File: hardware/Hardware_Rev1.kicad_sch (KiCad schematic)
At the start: 149 parts, among them J1 RJ45_LED_Shielded, J2 6P6C, Q1 BSS138, Q10 IRF7606PBF, Q11 IRF7606PBF, Q12 IRF7606PBF, Q13 BSS138, Q14 BSS138, Q15 BSS138, Q16 IRF7606PBF, Q17 IRF7606PBF, Q18 IRF7606PBF, Q19 BSS138, Q2 BSS138, Q20 BSS138, Q21 BSS138, Q22 IRF7606PBF, Q23 IRF7606PBF, Q24 IRF7606PBF, Q3 BSS138, Q4 IRF7606PBF, Q5 IRF7606PBF, Q6 IRF7606PBF, Q7 BSS138, Q8 BSS138, Q9 BSS138, U3 OKI, U5 TSR_1-2450, U6 Teensy4.1_DEV-16771

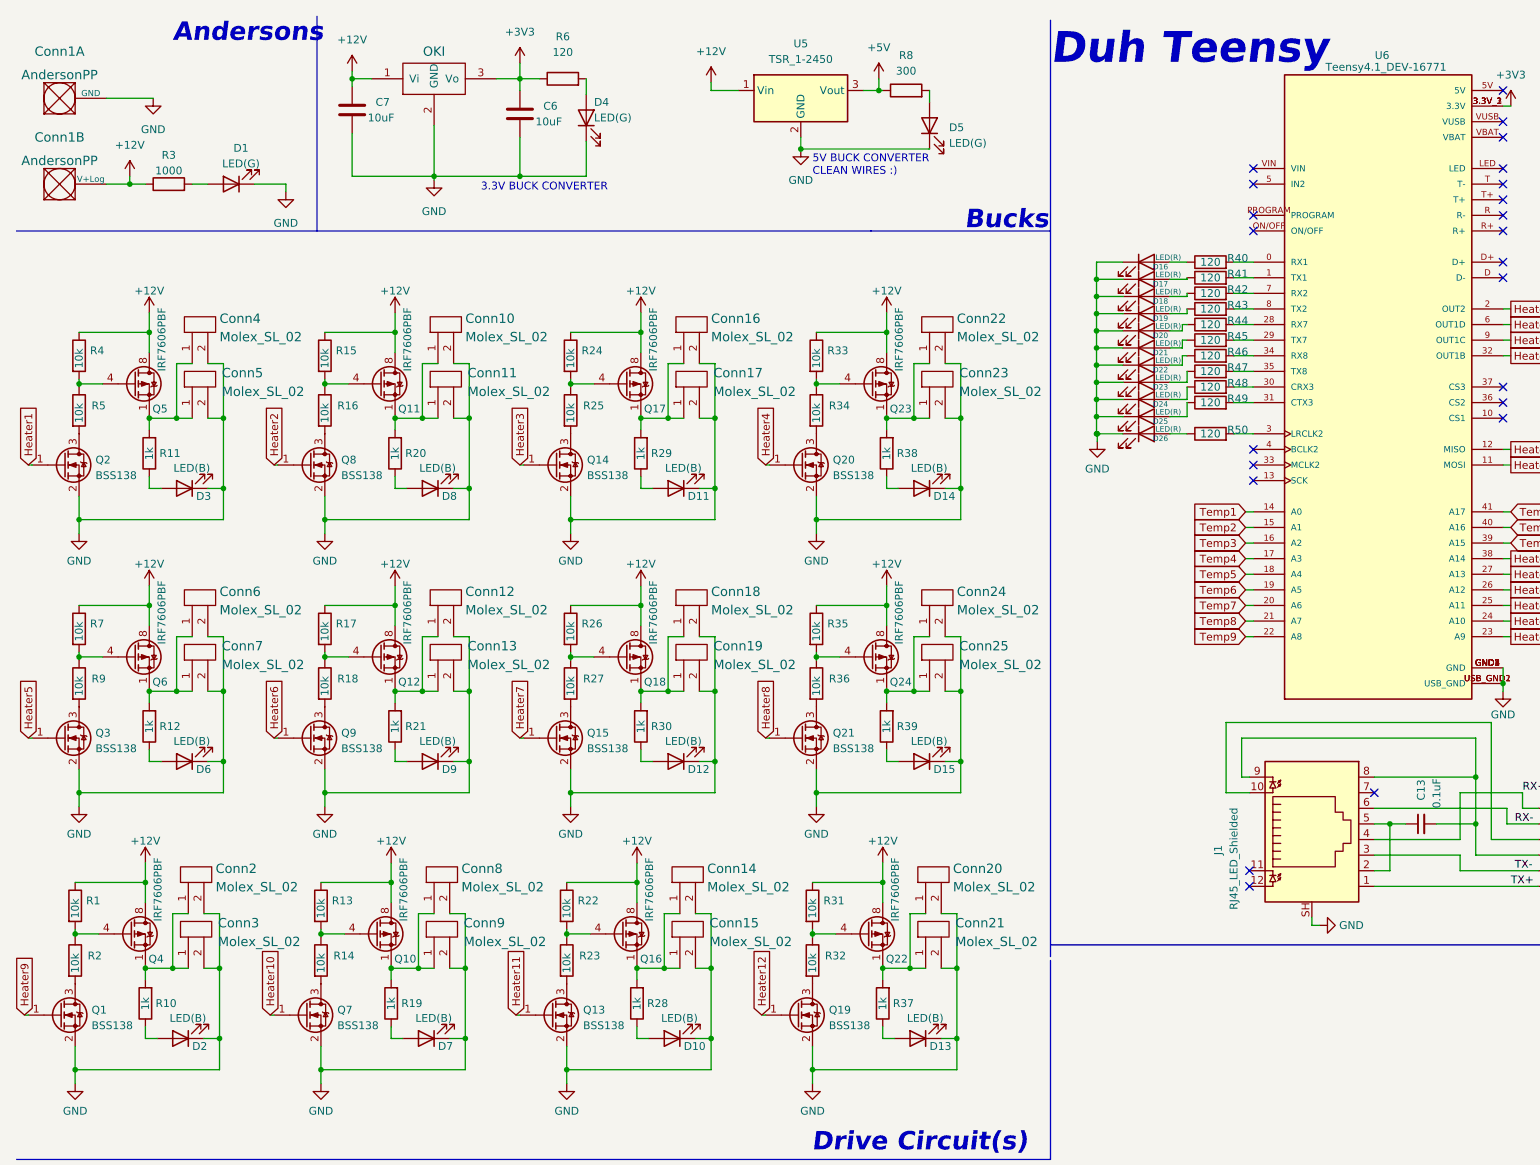
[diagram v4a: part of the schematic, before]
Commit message: Finished toggle circuits
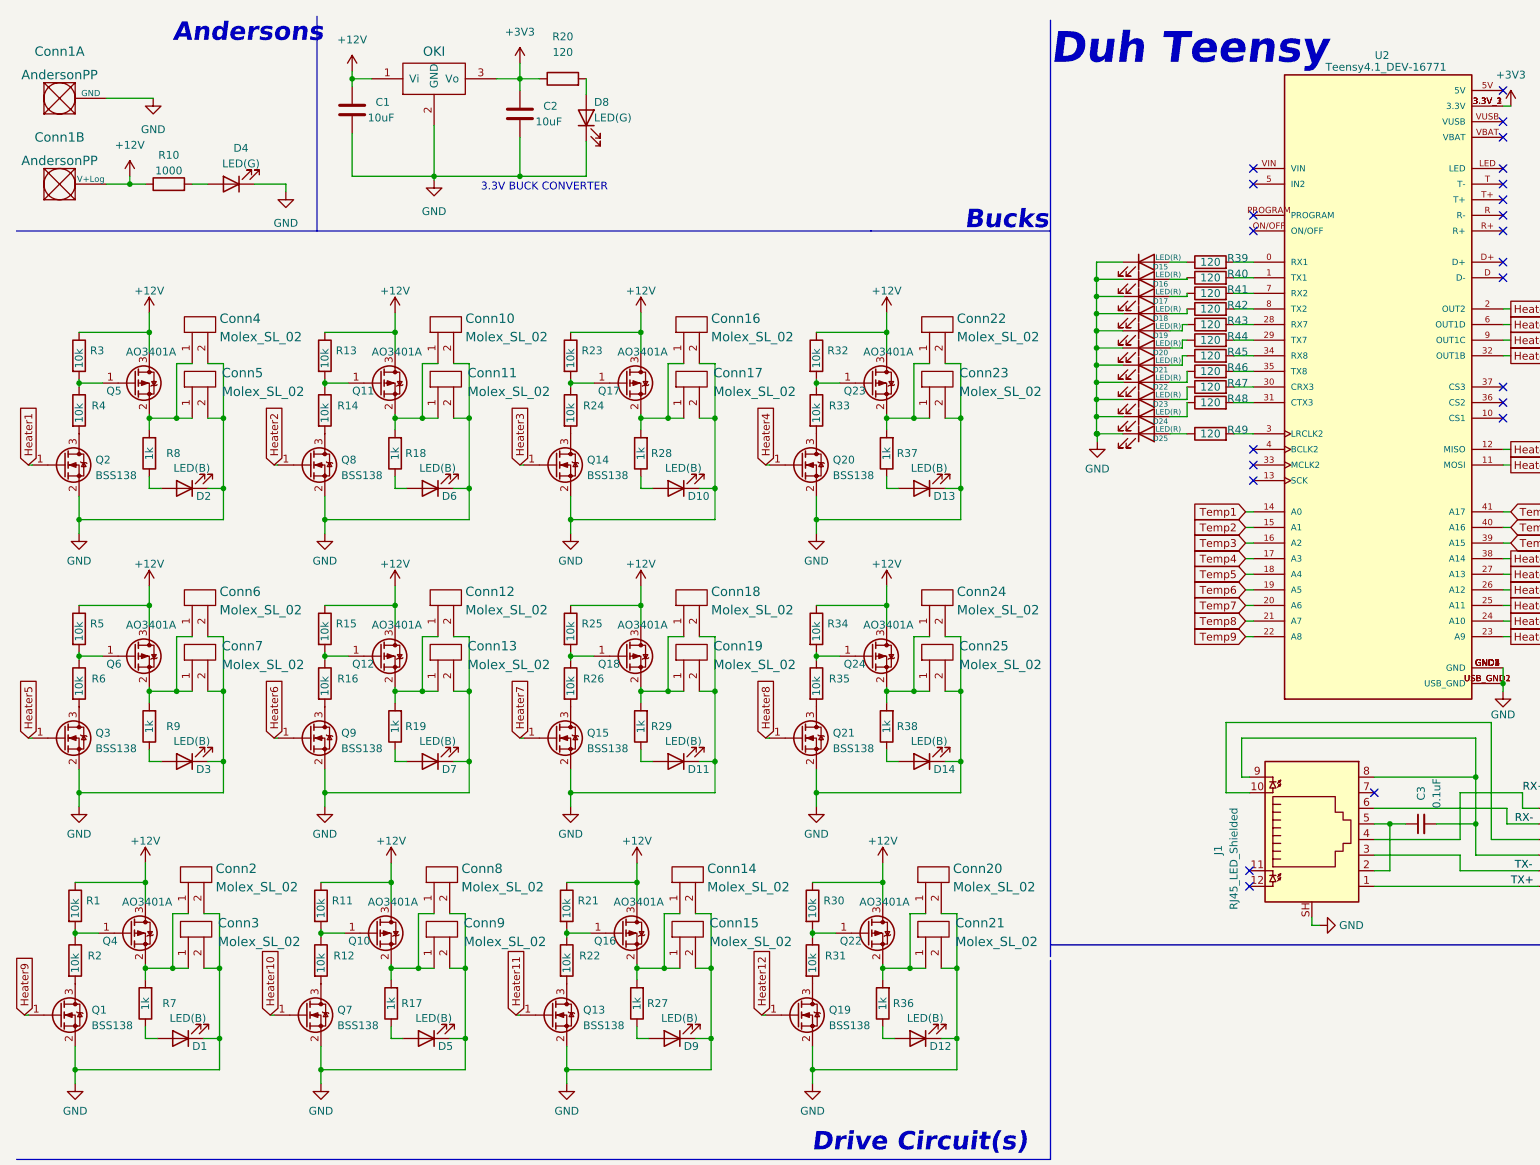
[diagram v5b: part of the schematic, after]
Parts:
- removed D5: LED(G), LED_SMD:LED_0603_1608Metric_Pad1.05x0.95mm_HandSolder, symbol Device:LED
- removed Q10, Q11, Q12, Q16, Q17, Q18, Q22, Q23, Q24, Q4, Q5, Q6: IRF7606PBF, Package_SO:MSOP-8_3x3mm_P0.65mm, symbol Transistor_FET:IRF7606PBF
- removed R8: 300, Resistor_SMD:R_0603_1608Metric_Pad0.98x0.95mm_HandSolder, symbol Device:R
- removed U5: TSR_1-2450, Converter_DCDC:Converter_DCDC_TRACO_TSR-1_THT, symbol Regulator_Switching:TSR_1-2450
- added Q10, Q11, Q12, Q16, Q17, Q18, Q22, Q23, Q24, Q4, Q5, Q6: AO3401A, Package_TO_SOT_SMD:SOT-23, symbol Transistor_FET:AO3401A
- renumbered C7 to C1, C6 to C2, C13 to C3, D2 to D1, D11 to D10, D12 to D11, D13 to D12, D14 to D13, D15 to D14, D16 to D15, D17 to D16, D18 to D17, D19 to D18, D20 to D19, D3 to D2, D21 to D20, D22 to D21, D23 to D22, D24 to D23, D25 to D24, D26 to D25, D6 to D3, D1 to D4, D7 to D5, D8 to D6, D9 to D7, D4 to D8, D10 to D9, R3 to R10, R13 to R11, R14 to R12, R15 to R13, R16 to R14, R17 to R15, R18 to R16, R19 to R17, R20 to R18, R21 to R19, R6 to R20, R22 to R21, R23 to R22, R24 to R23, R25 to R24, R26 to R25, R27 to R26, R28 to R27, R29 to R28, R30 to R29, R4 to R3, R31 to R30, R32 to R31, R33 to R32, R34 to R33, R35 to R34, R36 to R35, R37 to R36, R38 to R37, R39 to R38, R40 to R39, R5 to R4, R41 to R40, R42 to R41, R43 to R42, R44 to R43, R45 to R44, R46 to R45, R47 to R46, R48 to R47, R49 to R48, R50 to R49, R7 to R5, R9 to R6, R10 to R7, R11 to R8, R12 to R9, U3 to U1, U6 to U2
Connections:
- net +12V: now also Q10.3 (D), Q11.3 (D), Q12.3 (D), Q16.3 (D), Q17.3 (D), Q18.3 (D), Q22.3 (D), Q23.3 (D), Q24.3 (D), Q4.3 (D), Q5.3 (D), Q6.3 (D)
- net at R34.2, R35.1: now also Q24.1 (G)
- net at R21.2, R22.1: now also Q16.1 (G)
- net at R15.2, R16.1: now also Q12.1 (G)
- net at Conn22.1, Conn23.1, R37.2: now also Q23.2 (S)
- net at Conn8.1, Conn9.1, R17.2: now also Q10.2 (S)
- net at R3.2, R4.1: now also Q5.1 (G)
- net at Conn14.1, Conn15.1, R27.2: now also Q16.2 (S)
- net at R11.2, R12.1: now also Q10.1 (G)
- net at R1.2, R2.1: now also Q4.1 (G)
- net at Conn12.1, Conn13.1, R19.2: now also Q12.2 (S)
- net at Conn4.1, Conn5.1, R8.2: now also Q5.2 (S)
- net at Conn16.1, Conn17.1, R28.2: now also Q17.2 (S)
- net at R23.2, R24.1: now also Q17.1 (G)
- net at Conn6.1, Conn7.1, R9.2: now also Q6.2 (S)
- net at Conn20.1, Conn21.1, R36.2: now also Q22.2 (S)
- net at R32.2, R33.1: now also Q23.1 (G)
- net at R25.2, R26.1: now also Q18.1 (G)
- net at R5.2, R6.1: now also Q6.1 (G)
- net at R30.2, R31.1: now also Q22.1 (G)
- net at Conn10.1, Conn11.1, R18.2: now also Q11.2 (S)
- net at Conn2.1, Conn3.1, R7.2: now also Q4.2 (S)
- net at R13.2, R14.1: now also Q11.1 (G)
- net at Conn18.1, Conn19.1, R29.2: now also Q18.2 (S)
- net at Conn24.1, Conn25.1, R38.2: now also Q24.2 (S)
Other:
- note removed: "5V BUCK CONVERTER CLEAN WIRES :)"

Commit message: Finished connections
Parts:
- added D26: LED(R), LED_SMD:LED_0603_1608Metric_Pad1.05x0.95mm_HandSolder, symbol Device:LED
- added R50: 120, Resistor_SMD:R_0603_1608Metric_Pad0.98x0.95mm_HandSolder, symbol Device:R
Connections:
- net GND: now also D26.1 (K)
- net at U2.4 (BCLK2): now also R50.2
- new net: D26.2 (A), R50.1
- no-connect marks 23 -> 22
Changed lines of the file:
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@@
   (junction (at 187.833 77.216) (diameter 0) (color 0 0 0 0)
   )
+  (junction (at 187.96 82.55) (diameter 0) (color 0 0 0 0)
+  )
   (junction (at 73.66 63.5) (diameter 0) (color 0 0 0 0)
   )
@@
   (junction (at 102.235 93.98) (diameter 0) (color 0 0 0 0)
   )
-  (junction (at 187.96 80.01) (diameter 0) (color 0 0 0 0)
-  )
   (junction (at 125.095 167.005) (diameter 0) (color 0 0 0 0)
   )
@@
   (junction (at 33.655 63.5) (diameter 0) (color 0 0 0 0)
   )
-  (junction (at 187.833 80.01) (diameter 0) (color 0 0 0 0)
-  )
   (junction (at 153.035 153.035) (diameter 0) (color 0 0 0 0)
   )
@@
   (junction (at 45.72 121.92) (diameter 0) (color 0 0 0 0)
   )
+  (junction (at 187.96 80.01) (diameter 0) (color 0 0 0 0)
+  )
   (junction (at 22.225 116.205) (diameter 0) (color 0 0 0 0)
   )
@@
   (no_connect (at 254 31.75))
   (no_connect (at 254 29.21))
-  (no_connect (at 213.36 82.55))
   (no_connect (at 254 77.47))
   (no_connect (at 254 74.93))
@@
     (stroke (width 0) (type default) (color 0 0 0 0))
   )
+  (wire (pts (xy 187.96 80.01) (xy 187.96 82.55))
+    (stroke (width 0) (type default) (color 0 0 0 0))
+  )
   (wire (pts (xy 118.11 68.58) (xy 120.65 68.58))
     (stroke (width 0) (type default) (color 0 0 0 0))
@@
     (stroke (width 0) (type default) (color 0 0 0 0))
   )
+  (wire (pts (xy 192.151 82.55) (xy 187.96 82.55))
+    (stroke (width 0) (type default) (color 0 0 0 0))
+  )
   (wire (pts (xy 153.67 60.325) (xy 153.67 63.5))
     (stroke (width 0) (type default) (color 0 0 0 0))
@@
     (stroke (width 0) (type default) (color 0 0 0 0))
   )
+  (wire (pts (xy 199.771 82.55) (xy 202.565 82.55))
+    (stroke (width 0) (type default) (color 0 0 0 0))
+  )
   (wire (pts (xy 85.725 77.47) (xy 85.725 68.58))
     (stroke (width 0) (type default) (color 0 0 0 0))
@@
     (stroke (width 0) (type default) (color 0 0 0 0))
   )
-  (wire (pts (xy 187.96 80.01) (xy 187.833 80.01))
-    (stroke (width 0) (type default) (color 0 0 0 0))
-  )
   (wire (pts (xy 153.035 178.435) (xy 154.94 178.435))
     (stroke (width 0) (type default) (color 0 0 0 0))
@@
     (stroke (width 0) (type default) (color 0 0 0 0))
   )
+  (wire (pts (xy 210.185 82.55) (xy 213.36 82.55))
+    (stroke (width 0) (type default) (color 0 0 0 0))
+  )
   (wire (pts (xy 42.545 167.005) (xy 45.085 167.005))
     (stroke (width 0) (type default) (color 0 0 0 0))
@@
     (stroke (width 0) (type default) (color 0 0 0 0))
   )
-  (wire (pts (xy 187.96 80.01) (xy 187.96 81.28))
+  (wire (pts (xy 187.96 82.55) (xy 187.96 83.82))
     (stroke (width 0) (type default) (color 0 0 0 0))
   )
@@
     (stroke (width 0) (type default) (color 0 0 0 0))
   )
-  (wire (pts (xy 192.151 80.01) (xy 187.96 80.01))
+  (wire (pts (xy 187.833 80.01) (xy 187.96 80.01))
     (stroke (width 0) (type default) (color 0 0 0 0))
   )
@@
     (stroke (width 0) (type default) (color 0 0 0 0))
   )
+  (wire (pts (xy 187.96 80.01) (xy 192.151 80.01))
+    (stroke (width 0) (type default) (color 0 0 0 0))
+  )
   (wire (pts (xy 33.655 131.445) (xy 33.655 133.35))
     (stroke (width 0) (type default) (color 0 0 0 0))
@@
     (pin "1")
   )
+  (symbol (lib_id "Device:LED") (at 195.961 82.55 0) (unit 1)
+    (in_bom yes) (on_board yes)
+    (property "Reference" "D26" (id 0) (at 198.247 83.312 0)
+      (effects (font (size 0.889 0.889)))
+    )
+    (property "Value" "LED(R)" (id 1) (at 199.517 81.788 0)
+      (effects (font (size 0.889 0.889)))
+    )
+    (property "Footprint" "LED_SMD:LED_0603_1608Metric_Pad1.05x0.95mm_HandSolder" (id 2) (at 195.961 82.55 0)
+      (effects (font (size 1.27 1.27)) hide)
+    )
+    (property "Datasheet" "~" (id 3) (at 195.961 82.55 0)
+      (effects (font (size 1.27 1.27)) hide)
+    )
+    (pin "1")
+    (pin "2")
+  )
   (symbol (lib_id "power:GND") (at 337.82 89.535 0) (unit 1)
     (in_bom yes) (on_board yes) (fields_autoplaced)
@@
     (pin "1")
   )
-  (symbol (lib_id "power:GND") (at 187.96 81.28 0) (unit 1)
+  (symbol (lib_id "power:GND") (at 187.96 83.82 0) (unit 1)
     (in_bom yes) (on_board yes) (fields_autoplaced)
-    (property "Reference" "#PWR031" (id 0) (at 187.96 87.63 0)
+    (property "Reference" "#PWR031" (id 0) (at 187.96 90.17 0)
       (effects (font (size 1.27 1.27)) hide)
     )
-    (property "Value" "GND" (id 1) (at 187.96 85.7234 0))
-    (property "Footprint" "" (id 2) (at 187.96 81.28 0)
+    (property "Value" "GND" (id 1) (at 187.96 88.2634 0))
+    (property "Footprint" "" (id 2) (at 187.96 83.82 0)
       (effects (font (size 1.27 1.27)) hide)
     )
-    (property "Datasheet" "" (id 3) (at 187.96 81.28 0)
+    (property "Datasheet" "" (id 3) (at 187.96 83.82 0)
       (effects (font (size 1.27 1.27)) hide)
     )
@@
     (pin "2")
   )
+  (symbol (lib_id "Device:R") (at 206.375 82.55 90) (unit 1)
+    (in_bom yes) (on_board yes)
+    (property "Reference" "R50" (id 0) (at 210.82 81.915 90))
+    (property "Value" "120" (id 1) (at 206.375 82.55 90))
+    (property "Footprint" "Resistor_SMD:R_0603_1608Metric_Pad0.98x0.95mm_HandSolder" (id 2) (at 206.375 84.328 90)
+      (effects (font (size 1.27 1.27)) hide)
+    )
+    (property "Datasheet" "~" (id 3) (at 206.375 82.55 0)
+      (effects (font (size 1.27 1.27)) hide)
+    )
+    (pin "1")
+    (pin "2")
+  )
   (symbol (lib_id "Device:LED") (at 39.37 88.9 180) (unit 1)
     (in_bom yes) (on_board yes)
@@
       (reference "D25") (unit 1) (value "LED(R)") (footprint "LED_SMD:LED_0603_1608Metric_Pad1.05x0.95mm_HandSolder")
     )
+    (path "/6d949603-847f-4e56-b193-01912840b2f5"
+      (reference "D26") (unit 1) (value "LED(R)") (footprint "LED_SMD:LED_0603_1608Metric_Pad1.05x0.95mm_HandSolder")
+    )
     (path "/c2380cb7-4961-4052-bc8b-0b990bf9ca9f"
       (reference "J1") (unit 1) (value "RJ45_LED_Shielded") (footprint "MRDT_Connectors:RJ45_Teensy")
@@
       (reference "R49") (unit 1) (value "120") (footprint "Resistor_SMD:R_0603_1608Metric_Pad0.98x0.95mm_HandSolder")
     )
+    (path "/a6972e9c-2b36-4d0d-8530-9b703b7ced0d"
+      (reference "R50") (unit 1) (value "120") (footprint "Resistor_SMD:R_0603_1608Metric_Pad0.98x0.95mm_HandSolder")
+    )
     (path "/1a6178a5-56d4-4943-9131-ec94d86ded73"
